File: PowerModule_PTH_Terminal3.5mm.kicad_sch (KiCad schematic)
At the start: 3 parts, among them J1 Conn_01x05, J2 Conn_01x05, J3 Screw_Terminal

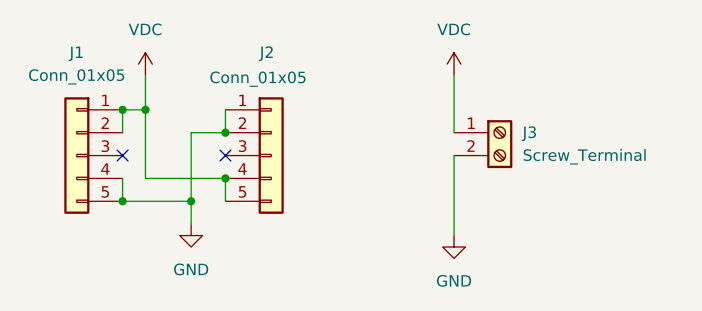
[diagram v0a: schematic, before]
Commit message: Fix the wrong side connectors
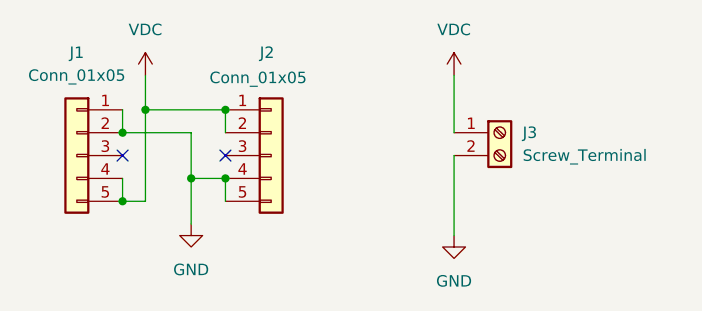
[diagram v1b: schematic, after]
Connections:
- net GND: now also J1.1 (Pin_1), J1.2 (Pin_2), J2.4 (Pin_4), J2.5 (Pin_5); no longer J1.4 (Pin_4), J1.5 (Pin_5), J2.1 (Pin_1), J2.2 (Pin_2)
- net VDC: now also J1.4 (Pin_4), J1.5 (Pin_5), J2.1 (Pin_1), J2.2 (Pin_2); no longer J1.1 (Pin_1), J1.2 (Pin_2), J2.4 (Pin_4), J2.5 (Pin_5)
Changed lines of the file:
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@@
 		(title "PlugAndPlay Power Module - 3.5mm Terminal Connector")
 		(date "2025-01-23")
-		(rev "1")
+		(rev "2")
 		(company "A.B. Yazamut")
 	)
 	(junction
-		(at 132.08 95.25)
+		(at 135.89 92.71)
+		(diameter 0)
+		(color 0 0 0 0)
+	)
+	(junction
+		(at 135.89 85.09)
+		(diameter 0)
+		(color 0 0 0 0)
+	)
+	(junction
+		(at 132.08 92.71)
 		(diameter 0)
 		(color 0 0 0 0)
@@
 	)
 	(junction
-		(at 124.46 95.25)
+		(at 124.46 87.63)
 		(diameter 0)
 		(color 0 0 0 0)
 	)
 	(junction
-		(at 135.89 87.63)
-		(diameter 0)
-		(color 0 0 0 0)
-	)
-	(junction
-		(at 124.46 85.09)
-		(diameter 0)
-		(color 0 0 0 0)
-	)
-	(junction
-		(at 135.89 92.71)
+		(at 124.46 95.25)
 		(diameter 0)
 		(color 0 0 0 0)
@@
 	(wire
 		(pts
-			(xy 132.08 97.79) (xy 132.08 95.25)
-		)
-		(stroke
-			(width 0)
-			(type default)
-		)
-	)
-	(wire
-		(pts
-			(xy 127 92.71) (xy 135.89 92.71)
+			(xy 132.08 92.71) (xy 132.08 87.63)
 		)
 		(stroke
@@
 	(wire
 		(pts
-			(xy 124.46 85.09) (xy 127 85.09)
+			(xy 135.89 92.71) (xy 135.89 95.25)
 		)
 		(stroke
@@
 	(wire
 		(pts
-			(xy 132.08 95.25) (xy 124.46 95.25)
+			(xy 127 85.09) (xy 135.89 85.09)
 		)
 		(stroke
@@
 	(wire
 		(pts
-			(xy 132.08 87.63) (xy 132.08 95.25)
+			(xy 132.08 92.71) (xy 135.89 92.71)
 		)
 		(stroke
@@
 	(wire
 		(pts
-			(xy 135.89 92.71) (xy 135.89 95.25)
+			(xy 132.08 87.63) (xy 124.46 87.63)
+		)
+		(stroke
+			(width 0)
+			(type default)
+		)
+	)
+	(wire
+		(pts
+			(xy 161.29 81.28) (xy 161.29 87.63)
+		)
+		(stroke
+			(width 0)
+			(type default)
+		)
+	)
+	(wire
+		(pts
+			(xy 132.08 97.79) (xy 132.08 92.71)
+		)
+		(stroke
+			(width 0)
+			(type default)
+		)
+	)
+	(wire
+		(pts
+			(xy 124.46 85.09) (xy 124.46 87.63)
 		)
 		(stroke
@@
 	(wire
 		(pts
-			(xy 161.29 81.28) (xy 161.29 87.63)
-		)
-		(stroke
-			(width 0)
-			(type default)
-		)
-	)
-	(wire
-		(pts
-			(xy 124.46 85.09) (xy 124.46 87.63)
-		)
-		(stroke
-			(width 0)
-			(type default)
-		)
-	)
-	(wire
-		(pts
-			(xy 127 85.09) (xy 127 92.71)
-		)
-		(stroke
-			(width 0)
-			(type default)
-		)
-	)
-	(wire
-		(pts
-			(xy 135.89 87.63) (xy 132.08 87.63)
+			(xy 127 95.25) (xy 124.46 95.25)
 		)
 		(stroke
@@
 		)
 		(stroke
+			(width 0)
+			(type default)
+		)
+	)
+	(wire
+		(pts
+			(xy 127 85.09) (xy 127 95.25)
+		)
+		(stroke
